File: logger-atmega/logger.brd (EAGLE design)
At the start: 60.6 x 26.7 mm, 28 parts, among them IC1 75176AD, IC2 REG1117, U1 MSP430G2352IPW14

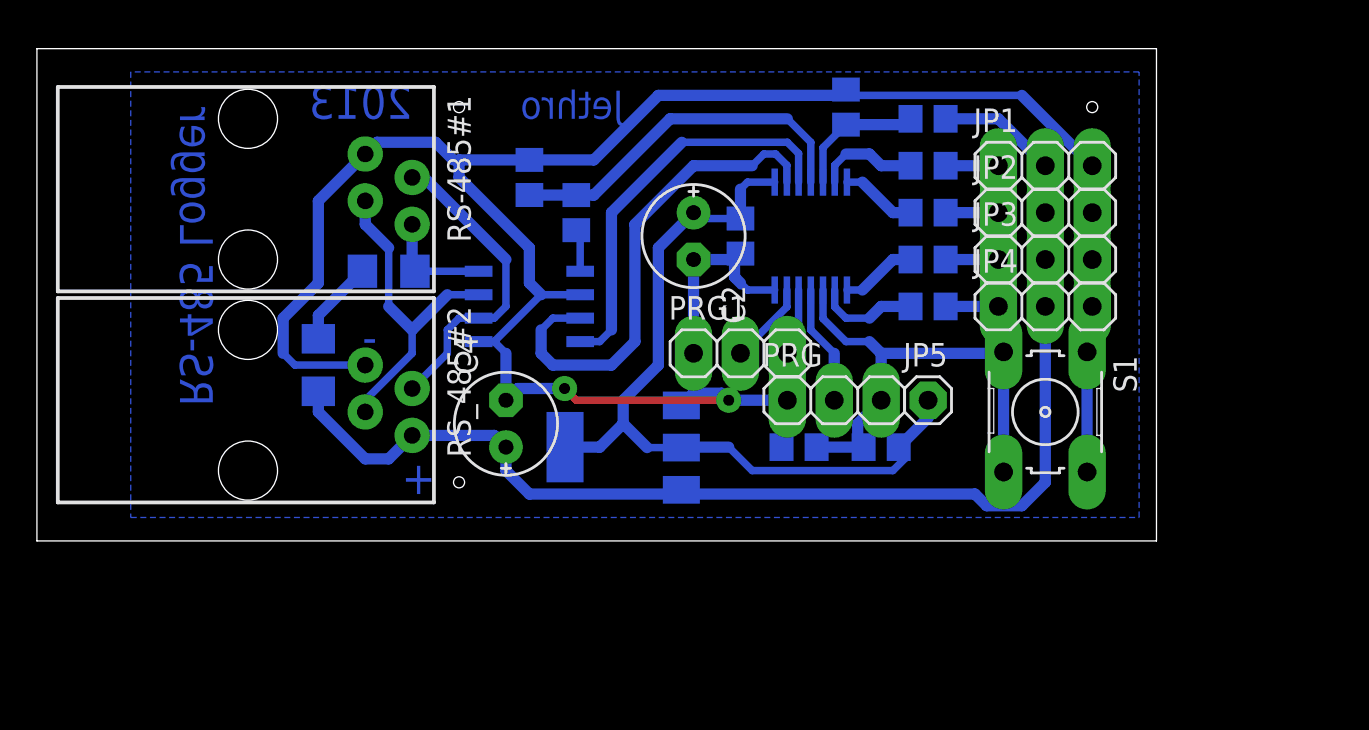
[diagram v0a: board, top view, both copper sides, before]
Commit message: ATMega logger routed.
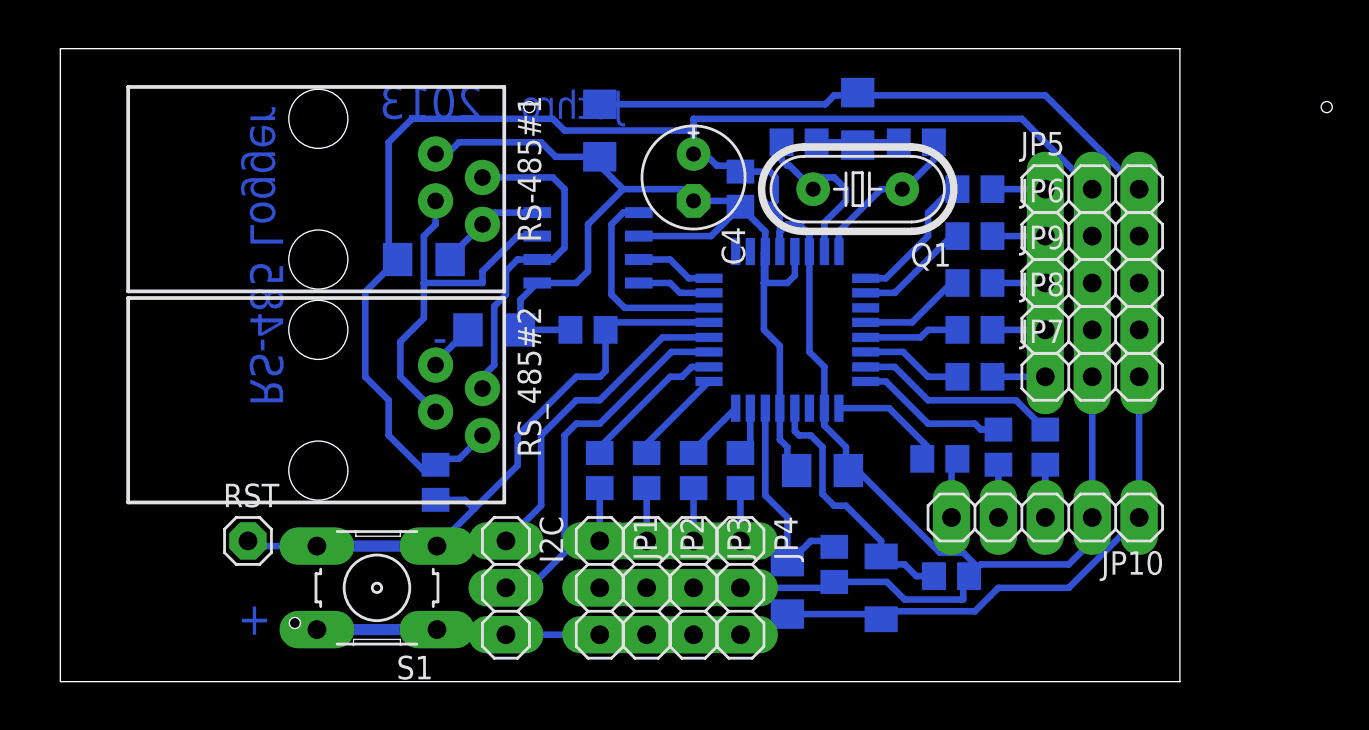
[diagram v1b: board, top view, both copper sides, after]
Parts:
- removed IC2: REG1117, burr-brown:SOT223
- removed PRG, PRG1: (no value), pinhead:1X03
- added C5, C6: (no value), rcl:C0805
- added D1: (no value), diode:SOD80C
- added I2C, JP6, JP7, JP8, JP9: (no value), pinhead:1X03
- added JP10: (no value), pinhead:1X05
- added Q1: (no value), crystal:HC49U-V
- added R13, R14, R15, R16, R17, R18, R7: (no value), rcl:R0805
- added R19, R20: (no value), rcl:R1206
- added RST: (no value), pinhead:1X01
- C1: device rcl:C0805 -> rcl:C1206
- C2: device rcl:E2,5-6E -> rcl:C0805
- JP5: device pinhead:1X01 -> pinhead:1X03
- R6: device rcl:R0805 -> rcl:R1206
- U1: value MSP430G2352IPW14 -> ATMEGA48PA-AU; device MSP430G2352IPW14:SOP65P640X120-14N -> atmega48PA:QFP80P900X900X120-32N
- moved S1 37.4 mm to (45.1, 45.7), turned to 180 degrees
- moved JP1 33.2 mm to (57.1, 45.7), turned to 270 degrees
- moved R10 32.1 mm to (71.1, 71.1)
- moved JP2 29.6 mm to (59.7, 45.7), turned to 270 degrees
- moved R6 26.2 mm to (67.3, 45.7), turned to 90 degrees
- moved JP3 26.1 mm to (62.2, 45.7), turned to 270 degrees
- moved R11 25.5 mm to (77.5, 59.7), turned to 0 degrees
- moved R5 24.7 mm to (69.8, 47.0), turned to 270 degrees
- moved R1 24.3 mm to (57.1, 52.1), turned to 270 degrees
- moved R8 24.2 mm to (48.3, 51.4), turned to 270 degrees
- moved JP4 22.5 mm to (64.8, 45.7), turned to 270 degrees
- moved R12 21.9 mm to (77.5, 62.2), turned to 0 degrees
- moved R2 20.7 mm to (59.7, 52.1), turned to 270 degrees
- moved R3 17.1 mm to (62.2, 52.1), turned to 270 degrees
- moved C4 16.8 mm to (62.2, 67.9), turned to 270 degrees
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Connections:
- removed net +3V3: C1.2, C2.+, IC2.2, IC2.4, JP5.1, R8.1, U1.1
- removed net N$19: R10.1, R9.2
- new net DE: IC1.3, U1.32
- new net N$17: JP10.3, R13.2
- new net N$23: JP8.1, R11.1
- new net N$24: JP7.1, R7.1
- new net N$25: R13.1, U1.15
- new net N$26: R14.1, U1.16
- new net N$27: R16.1, U1.9
- new net N$28: R17.1, U1.10
- new net N$29: R15.1, U1.17
- new net N$30: R19.2, RS_485#2.1
- new net N$31: R12.2, U1.12
- new net N$32: R11.2, U1.13
- new net N$33: R7.2, U1.14
- new net N$34: D1.C, R18.1, U1.20
- new net N$35: C2.2, C5.2, R10.2
- new net N$36: JP6.1, R17.2
- new net N$37: JP5.1, R16.2
- new net RX: IC1.1, U1.30
- new net TX: IC1.4, U1.31
- net +5V: now also C1.2, C6.2, JP10.2, JP5.2, JP6.2, JP7.2, JP8.2, JP9.2, R18.2, R8.1, R9.2, U1.18, U1.4, U1.6; no longer IC2.3, R10.2
- net GND: now also C6.1, D1.A, I2C.3, JP10.1, JP5.3, JP6.3, JP7.3, JP8.3, JP9.3, R10.1, R19.1, R20.1, R20.2, U1.21, U1.3, U1.5; no longer C2.-, IC2.1, PRG.1, PRG1.1, R11.2, RS_485#2.1, U1.14
- net N$10: now also U1.25; no longer U1.7
- net N$11: now also U1.26; no longer U1.6
- net N$12: now also JP9.1, R12.1; no longer PRG1.2, U1.13
- net N$13: now also JP10.5, R15.2; no longer IC1.4, U1.3
- net N$14: now also JP10.4, R14.2; no longer IC1.3, U1.2
- net N$15: now also RST.1, U1.29; no longer PRG.3, U1.10
- net N$16: now also C2.1, Q1.2, U1.7; no longer PRG.2, U1.11
- net N$18: now also C5.1, Q1.1, U1.8; no longer PRG1.3, U1.12
- net N$21: now also I2C.1, U1.28; no longer IC1.1, R12.1
- net N$22: now also I2C.2, U1.27; no longer R11.1, R12.2, U1.4
- net N$3: now also U1.22; no longer U1.5
- net N$4: now also U1.23; no longer U1.9
- net N$9: now also U1.24; no longer U1.8
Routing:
- net +5V: track 76.3 -> 147.6 mm
- net +3V3: track 43.5 -> 0.00 mm
- net GND: track 131.4 -> 157.1 mm, vias 2 -> 0
- net N$14: track 26.8 -> 2.86 mm
- net N$13: track 21.8 -> 3.31 mm
- net N$21: track 2.31 -> 17.8 mm
- net N$34: track 0.00 -> 14.0 mm
- net N$25: track 0.00 -> 11.1 mm
- net RX: track 0.00 -> 11.1 mm
- net N$26: track 0.00 -> 8.27 mm
- net N$15: track 26.9 -> 34.6 mm
- net N$27: track 0.00 -> 7.71 mm
- net N$35: track 0.00 -> 6.74 mm
- net N$29: track 0.00 -> 6.46 mm
- net N$28: track 0.00 -> 6.24 mm
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- removed copper zone on layer 16, net GND
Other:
- board size 60.6 x 26.7 mm -> 60.6 x 34.3 mm

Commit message: Upravy desky i schematu, snad definitivni.
Odebrana zenerka, budu verit vnitrni referenci
Pridana civka na analogovou zem
Pridan napajeci konektor

Napajeci cesty rozsireny
Doplneny napisy
Vylito medi
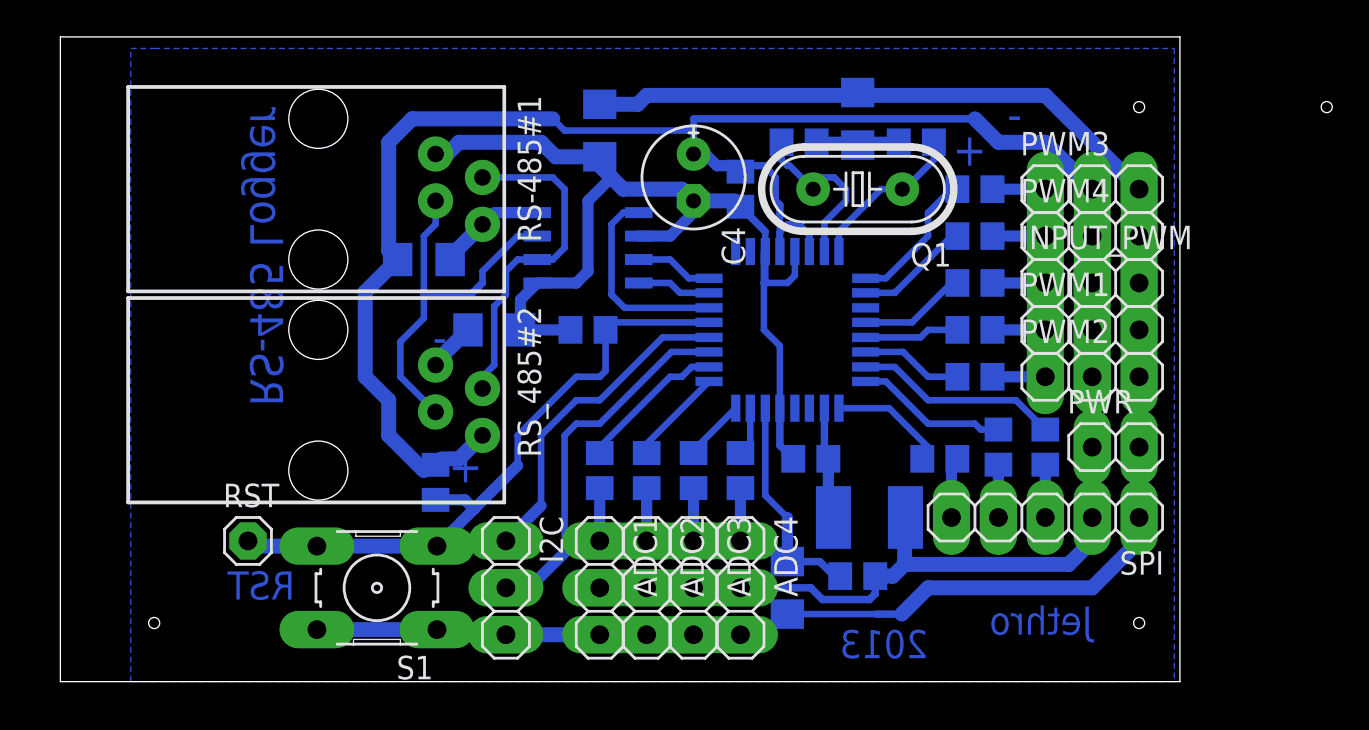
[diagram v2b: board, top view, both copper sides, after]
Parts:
- removed D1: (no value), diode:SOD80C
- removed R18: (no value), rcl:R0805
- added L1: 10uH, rcl:L1812
- added PWR: (no value), pinhead:1X02
- C1: value (none) -> 100n; device rcl:C1206 -> rcl:C0805
- C2, C5: value (none) -> 22p
- C6: value (none) -> 100n
- Q1: value (none) -> 10MHz
- R10, R19, R20, R9: value (none) -> 0R
- moved R5 1.42 mm to (71.1, 46.4), turned to 180 degrees
- moved C1 0.90 mm to (68.6, 52.7)
- renumbered JP1 to ADC1, JP10 to SPI, JP2 to ADC2, JP3 to ADC3, JP4 to ADC4, JP5 to PWM3, JP6 to PWM4, JP7 to PWM2, JP8 to PWM1, JP9 to INPUT_PWM
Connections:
- removed net N$34: D1.C, R18.1, U1.20
- new net N$19: C1.2, L1.2, U1.18
- net +5V: now also L1.1, PWR.1; no longer C1.2, R18.2, U1.18
- net GND: now also PWR.2; no longer D1.A
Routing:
- net +5V: track 147.6 -> 130.2 mm
- net N$34: track 14.0 -> 0.00 mm
- net N$19: track 0.00 -> 6.12 mm
- net GND: track 157.1 -> 155.2 mm
- added copper zone on layer 16, net GND
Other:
- board size 60.6 x 34.3 mm -> 60.6 x 34.9 mm
- board text added: "RST"

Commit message: Pridan kondenzator na AREF
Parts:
- removed L1: 10uH, rcl:L1812
- added C7: 100n, rcl:C0805
- added L2: 10uH, rcl:L1206
- moved C1 2.54 mm to (68.6, 50.2)
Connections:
- new net N$34: C7.2, U1.20
- net +5V: now also L2.1; no longer L1.1
- net GND: now also C7.1
- net N$19: now also L2.2; no longer L1.2
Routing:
- net GND: track 155.2 -> 161.1 mm
- net N$34: track 0.00 -> 3.87 mm
- net N$19: track 6.12 -> 9.34 mm
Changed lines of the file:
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@@
 <text x="80.01" y="70.485" size="1.778" layer="16" font="vector" rot="MR0">-</text>
 <rectangle x1="64.77" y1="57.15" x2="69.85" y2="63.5" layer="42"/>
-<rectangle x1="67.31" y1="50.165" x2="68.58" y2="51.435" layer="42"/>
 </plain>
 <attributes>
@@
 <element name="R5" library="rcl" package="R0805" value="" x="71.12" y="46.355" rot="MR180"/>
 <element name="R6" library="rcl" package="R1206" value="" x="67.31" y="45.72" rot="MR90"/>
-<element name="C1" library="rcl" package="C0805" value="100n" x="68.58" y="52.705" rot="MR180"/>
+<element name="C1" library="rcl" package="C0805" value="100n" x="68.58" y="50.165" rot="MR180"/>
 <element name="I2C" library="pinhead" package="1X03" value="" x="52.07" y="45.72" rot="R270"/>
 <element name="S1" library="switch-omron" package="B3F-10XX" value="" x="45.085" y="45.72" rot="R180">
@@
 <element name="R10" library="rcl" package="R1206" value="0R" x="71.12" y="71.12" rot="MR270"/>
 <element name="R20" library="rcl" package="R1206" value="0R" x="57.15" y="70.485" rot="MR90"/>
-<element name="L1" library="rcl" package="L1812" value="10uH" x="71.755" y="49.53" rot="MR0"/>
 <element name="PWR" library="pinhead" package="1X02" value="" x="85.09" y="53.34"/>
+<element name="C7" library="rcl" package="C0805" value="100n" x="68.58" y="52.705" rot="MR180"/>
+<element name="L2" library="rcl" package="L1206" value="10uH" x="72.39" y="50.165" rot="MR90"/>
 </elements>
 <signals>
@@
 <contactref element="SPI" pad="2"/>
 <wire x1="83.82" y1="57.15" x2="83.82" y2="53.34" width="0.8128" layer="16"/>
-<wire x1="83.82" y1="50.8" x2="83.82" y2="49.53" width="0.8128" layer="16"/>
 <wire x1="57.15" y1="45.72" x2="59.69" y2="45.72" width="0.8128" layer="16"/>
 <wire x1="59.69" y1="45.72" x2="62.23" y2="45.72" width="0.8128" layer="16"/>
@@
 <wire x1="54.61" y1="71.12" x2="55.245" y2="70.485" width="0.358" layer="16"/>
 <wire x1="55.245" y1="70.485" x2="62.23" y2="70.485" width="0.358" layer="16"/>
-<contactref element="L1" pad="1"/>
 <contactref element="C6" pad="2"/>
 <wire x1="64.45" y1="68.58" x2="64.77" y2="68.58" width="0.4064" layer="16"/>
@@
 <wire x1="72.07" y1="46.355" x2="73.025" y2="46.355" width="0.8128" layer="16"/>
 <wire x1="73.025" y1="46.355" x2="73.66" y2="46.99" width="0.8128" layer="16"/>
-<wire x1="73.66" y1="46.99" x2="73.66" y2="49.485" width="0.8128" layer="16"/>
-<wire x1="73.66" y1="49.485" x2="73.705" y2="49.53" width="0.4064" layer="16"/>
 <wire x1="71.755" y1="45.085" x2="72.07" y2="45.4" width="0.4064" layer="16"/>
 <wire x1="72.07" y1="45.4" x2="72.07" y2="46.355" width="0.4064" layer="16"/>
@@
 <wire x1="81.28" y1="69.85" x2="83.82" y2="67.31" width="0.8128" layer="16"/>
 <contactref element="PWR" pad="1"/>
-<wire x1="83.82" y1="53.34" x2="83.82" y2="50.8" width="0.8128" layer="16"/>
+<wire x1="83.82" y1="53.34" x2="83.82" y2="49.53" width="0.8128" layer="16"/>
+<contactref element="L2" pad="1"/>
+<wire x1="72.39" y1="48.765" x2="72.39" y2="48.26" width="0.4064" layer="16"/>
+<wire x1="72.39" y1="48.26" x2="73.66" y2="46.99" width="0.4064" layer="16"/>
 </signal>
 <signal name="GND">
@@
 <wire x1="64.77" y1="66.36" x2="66.1162" y2="65.0138" width="0.4064" layer="16"/>
 <wire x1="64.77" y1="66.36" x2="64.455" y2="66.675" width="0.4064" layer="16"/>
-<wire x1="66.9036" y1="55.4482" x2="66.9036" y2="53.4314" width="0.4064" layer="16"/>
-<wire x1="66.9036" y1="53.4314" x2="67.63" y2="52.705" width="0.4064" layer="16"/>
 <wire x1="83.82" y1="45.72" x2="74.93" y2="45.72" width="0.8128" layer="16"/>
 <wire x1="72.112" y1="44.298" x2="73.508" y2="44.298" width="0.4064" layer="16"/>
@@
 <vertex x="31.75" y="74.93"/>
 </polygon>
+<contactref element="C7" pad="1"/>
+<wire x1="66.9036" y1="58.8264" x2="66.9036" y2="53.4314" width="0.4064" layer="16"/>
+<wire x1="66.9036" y1="53.4314" x2="67.63" y2="52.705" width="0.4064" layer="16"/>
+<wire x1="67.63" y1="50.165" x2="67.63" y2="52.705" width="0.4064" layer="16"/>
 <wire x1="57.15" y1="69.063" x2="57.15" y2="71.907" width="0" layer="19" extent="16-16"/>
 </signal>
@@
 <contactref element="R6" pad="2"/>
 <contactref element="R5" pad="1"/>
-<wire x1="66.1162" y1="55.4482" x2="66.1162" y2="50.7238" width="0.358" layer="16"/>
-<wire x1="66.1162" y1="50.7238" x2="67.31" y2="49.53" width="0.358" layer="16"/>
-<wire x1="67.31" y1="49.53" x2="67.31" y2="47.142" width="0.6096" layer="16"/>
 <wire x1="67.31" y1="47.142" x2="69.063" y2="47.142" width="0.4064" layer="16"/>
 <wire x1="69.063" y1="47.142" x2="69.85" y2="46.355" width="0.4064" layer="16"/>
 <wire x1="69.85" y1="46.355" x2="70.17" y2="46.355" width="0.4064" layer="16"/>
+<wire x1="66.1162" y1="55.4482" x2="66.1162" y2="49.4538" width="0.4064" layer="16"/>
+<wire x1="66.1162" y1="49.4538" x2="67.31" y2="48.26" width="0.4064" layer="16"/>
+<wire x1="67.31" y1="48.26" x2="67.31" y2="47.142" width="0.4064" layer="16"/>
 </signal>
 <signal name="N$4">
@@
 </signal>
 <signal name="N$19">
-<contactref element="L1" pad="2"/>
 <contactref element="C1" pad="2"/>
 <contactref element="U1" pad="18"/>
-<wire x1="69.3166" y1="55.4482" x2="69.3166" y2="52.9184" width="0.4064" layer="16"/>
-<wire x1="69.3166" y1="52.9184" x2="69.53" y2="52.705" width="0.4064" layer="16"/>
-<wire x1="69.53" y1="52.705" x2="69.53" y2="49.805" width="0.6096" layer="16"/>
-<wire x1="69.53" y1="49.805" x2="69.805" y2="49.53" width="0.4064" layer="16"/>
+<contactref element="L2" pad="2"/>
+<wire x1="69.3166" y1="55.4482" x2="69.3166" y2="54.5084" width="0.4064" layer="16"/>
+<wire x1="69.3166" y1="54.5084" x2="69.85" y2="53.975" width="0.4064" layer="16"/>
+<wire x1="69.85" y1="53.975" x2="71.12" y2="53.975" width="0.4064" layer="16"/>
+<wire x1="72.39" y1="52.705" x2="72.39" y2="51.565" width="0.4064" layer="16"/>
+<wire x1="69.53" y1="50.165" x2="69.85" y2="50.165" width="0.4064" layer="16"/>
+<wire x1="69.85" y1="50.165" x2="71.12" y2="51.435" width="0.4064" layer="16"/>
+<wire x1="71.12" y1="51.435" x2="72.26" y2="51.435" width="0.4064" layer="16"/>
+<wire x1="72.26" y1="51.435" x2="72.39" y2="51.565" width="0.4064" layer="16"/>
+<wire x1="72.39" y1="52.705" x2="71.12" y2="53.975" width="0.4064" layer="16"/>
+</signal>
+<signal name="N$34">
+<contactref element="C7" pad="2"/>
+<contactref element="U1" pad="20"/>
+<wire x1="67.7164" y1="55.4482" x2="67.7164" y2="54.2036" width="0.4064" layer="16"/>
+<wire x1="67.7164" y1="54.2036" x2="67.945" y2="53.975" width="0.4064" layer="16"/>
+<wire x1="67.945" y1="53.975" x2="68.58" y2="53.975" width="0.4064" layer="16"/>
+<wire x1="68.58" y1="53.975" x2="69.215" y2="53.34" width="0.4064" layer="16"/>
+<wire x1="69.215" y1="53.34" x2="69.215" y2="53.02" width="0.4064" layer="16"/>
+<wire x1="69.215" y1="53.02" x2="69.53" y2="52.705" width="0.4064" layer="16"/>
 </signal>
 </signals>
